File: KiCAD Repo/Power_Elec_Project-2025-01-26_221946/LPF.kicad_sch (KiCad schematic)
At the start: 7 parts, among them U1 LM358

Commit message: lpf design
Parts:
- removed C3: C, symbol Device:C
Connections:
- net at L1.2, U1.3 (+): now also R1.1
- net at C2.1, L1.1, R2.1: no longer R1.1
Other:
- note added: "Exoecting a Quiescent output of 30V. The output of the opamp is between 0v to 3.3v Therefore R1 and R2 should generate the gain to scale 30v down to 3.3v/2 = 1.65v"
- note removed: "Exoecting a Quiescent output of 30V. The output of the opamp is between 0v to 3.3v Therefore R1 and R2 should generate the gain to scale 30v down to 3.3v/2 = 1.65v If R1 = 10k, R2~= 172k"
- moved on the sheet: C1, C2, L1, R1, R2, U1A, U1B, U1C

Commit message: gate driver import
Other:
- note added: "Expecting a Quiescent input of 30V. The output of the opamp is between 0v to 3.3v Therefore R1 and R2 should generate the gain to scale 30v down to 3.3v/2 = 1.65v"
- note added: "Opamp Power"
- note added: "Power IO"
- note added: "RLC LFP"
- note added: "Unused"
- note removed: "Exoecting a Quiescent output of 30V. The output of the opamp is between 0v to 3.3v Therefore R1 and R2 should generate the gain to scale 30v down to 3.3v/2 = 1.65v"
- moved on the sheet: C1, C2, L1, R1, R2, U1A, U1B, U1C

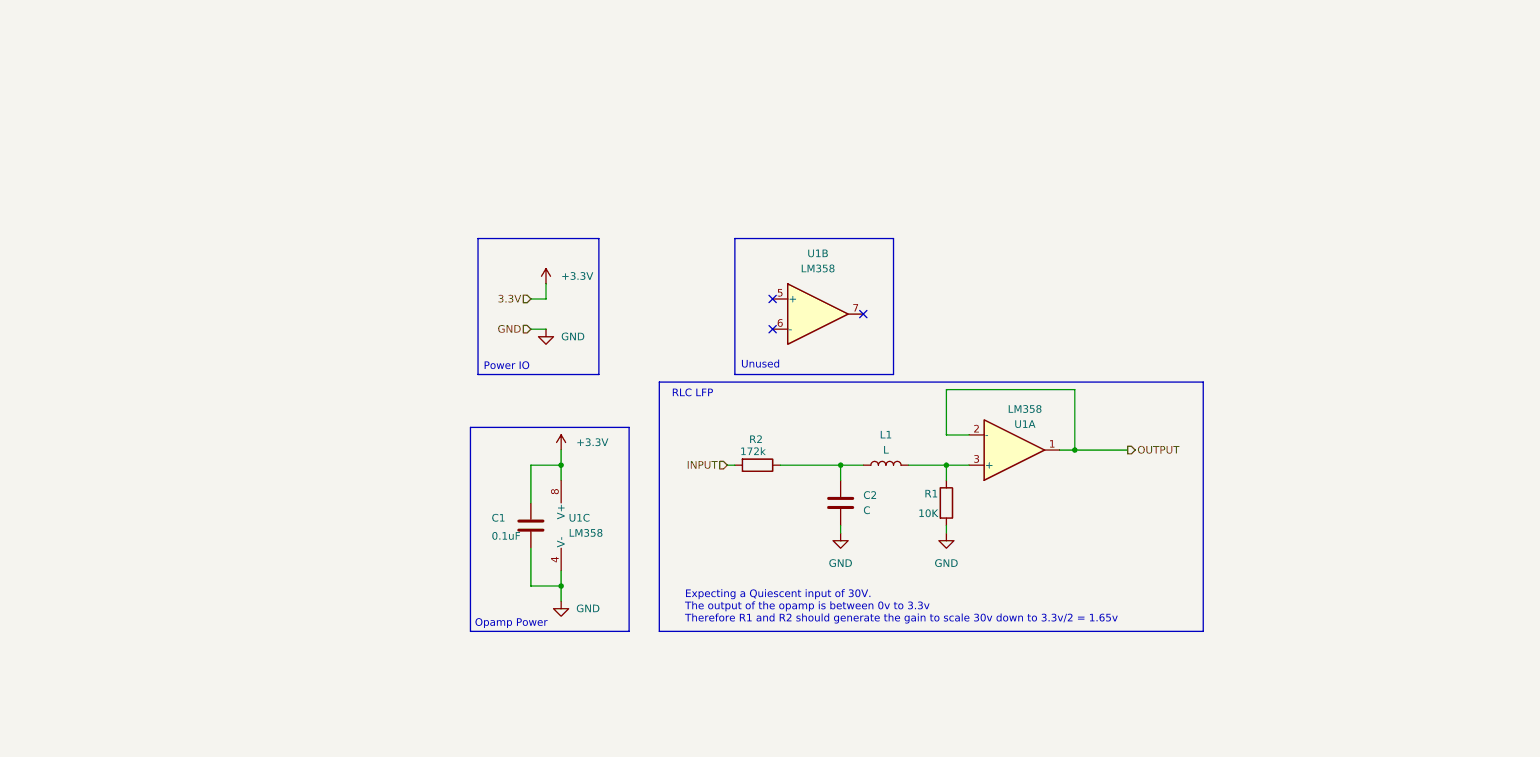
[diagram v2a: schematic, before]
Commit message: PLF and GD circuit
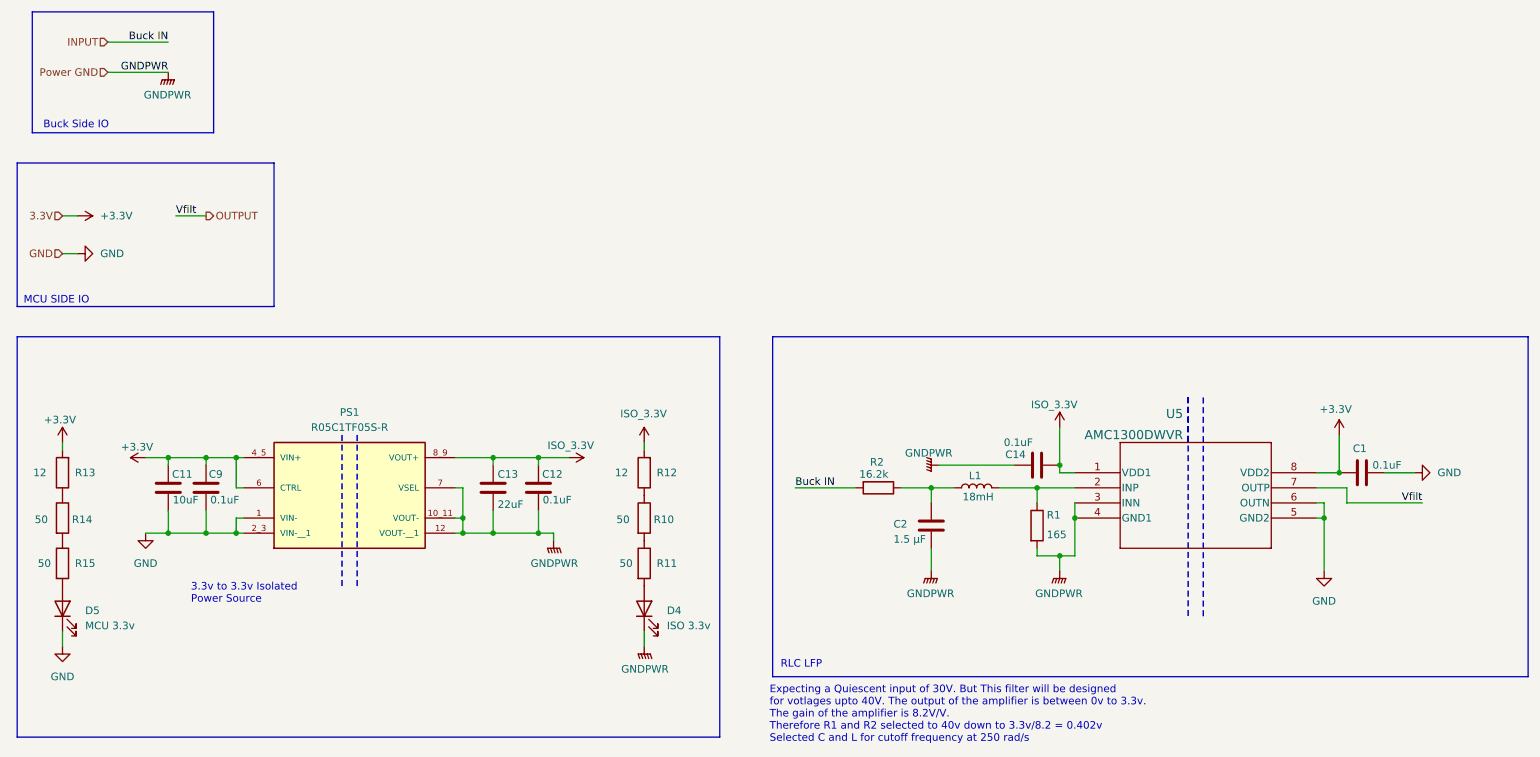
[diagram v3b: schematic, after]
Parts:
- removed U1: LM358, Package_SO:VSSOP-8_3x3mm_P0.65mm, symbol Amplifier_Operational:LM358
- added C11: 10uF, Capacitor_SMD:C_0603_1608Metric, symbol Device:C
- added C12, C14, C9: 0.1uF, Capacitor_SMD:C_0603_1608Metric, symbol Device:C
- added C13: 22uF, Capacitor_SMD:C_0603_1608Metric, symbol Device:C
- added D4: ISO 3.3v, LED_SMD:LED_0603_1608Metric, symbol Device:LED
- added D5: MCU 3.3v, LED_SMD:LED_0603_1608Metric, symbol Device:LED
- added PS1: R05C1TF05S-R, R05C1TF05S-R:CONV_R05C1TF05S-R, symbol R05C1TF05S-R:R05C1TF05S-R
- added R10, R11, R14, R15: 50, Resistor_SMD:R_0603_1608Metric, symbol Device:R
- added R12, R13: 12, Resistor_SMD:R_0805_2012Metric_Pad1.20x1.40mm_HandSolder, symbol Device:R
- added U5: AMC1300DWVR, DWV8_TEX, symbol Opamp AMC1300DWVR:AMC1300DWVR
- C1: footprint (none) -> Capacitor_SMD:C_0603_1608Metric; Part Number (none) -> C0603Y5V160-104ZNE
- C2: value C -> 1.5 µF; footprint (none) -> Capacitor_SMD:C_0805_2012Metric; Part Number (none) -> CC0805ZRY5V7BB155
- L1: value L -> 18mH; footprint (none) -> Inductor_THT:L_Radial_D12.0mm_P6.00mm_Murata_1900R; Part Number (none) -> 6100-183K-RC
- R1: value 10K -> 165; footprint Resistor_SMD:R_0805_2012Metric -> Resistor_SMD:R_0603_1608Metric; Part Number (none) -> ERJ-3EKF1650V
- R2: value 172k -> 16.2k; Part Number RNCF0603BKE172K -> CR161622F
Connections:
- net +3.3V: now also C1.2, C11.1, C9.1, PS1.4_5 (VIN+), PS1.6 (CTRL), R13.2, U5.8 (VDD2); no longer C1.1
- net GND: now also C1.1, C11.2, C9.2, D5.1 (K), PS1.1 (VIN-), PS1.2_3 (VIN-__1), U5.5 (GND2), U5.6 (OUTN); no longer C1.2, C2.2, R1.2
- net OUTPUT: now also U5.7 (OUTP)
- net at L1.2, R1.1: now also U5.2 (INP)
- new net: D4.2 (A), R11.2
- new net: R13.1, R14.1
- new net: R10.1, R12.1
- new net: R10.2, R11.1
- new net: R14.2, R15.1
- new net: D5.2 (A), R15.2
- new net GNDPWR: C12.2, C13.2, C14.2, C2.2, D4.1 (K), PS1.10_11 (VOUT-), PS1.12 (VOUT-__1), PS1.7 (VSEL), R1.2, U5.3 (INN), U5.4 (GND1)
- new net ISO_3.3V: C12.1, C13.1, C14.1, PS1.8_9 (VOUT+), R12.2, U5.1 (VDD1)
- no-connect marks 3 -> 0
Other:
- note added: "3.3v to 3.3v Isolated Power Source"
- note added: "Buck Side IO"
- note added: "Expecting a Quiescent input of 30V. But This filter will be designed for votlages upto 40V. The output of the amplifier is between 0v to 3.3v. The gain of the amplifier is 8.2V/V. Therefore R1 and R2 selected to 40v down to 3.3v/8.2 = 0.402v Selected C and L for cutoff frequency at 250 rad/s"
- note added: "MCU SIDE IO"
- note removed: "Expecting a Quiescent input of 30V. The output of the opamp is between 0v to 3.3v Therefore R1 and R2 should generate the gain to scale 30v down to 3.3v/2 = 1.65v"
- note removed: "Opamp Power"
- note removed: "Power IO"
- note removed: "Unused"
- company: (none) -> M.Nguyen B.Patel S.Dupuis
- moved on the sheet: C1, C2, L1, R1, R2

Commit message: PCB layout
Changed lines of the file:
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@@
 	(wire
 		(pts
-			(xy 147.32 105.41) (xy 157.48 105.41)
+			(xy 146.05 105.41) (xy 157.48 105.41)
 		)
 		(stroke
@@
 	)
 	(label "Buck IN"
-		(at 147.32 105.41 0)
-		(effects
-			(font
+		(at 146.05 105.41 0)
+		(effects
+			(font
